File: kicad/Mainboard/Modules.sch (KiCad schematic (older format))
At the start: 14 parts, among them U12 GD25Q16CSIGTR, U14 ESP8266EX, Y1 24MHz

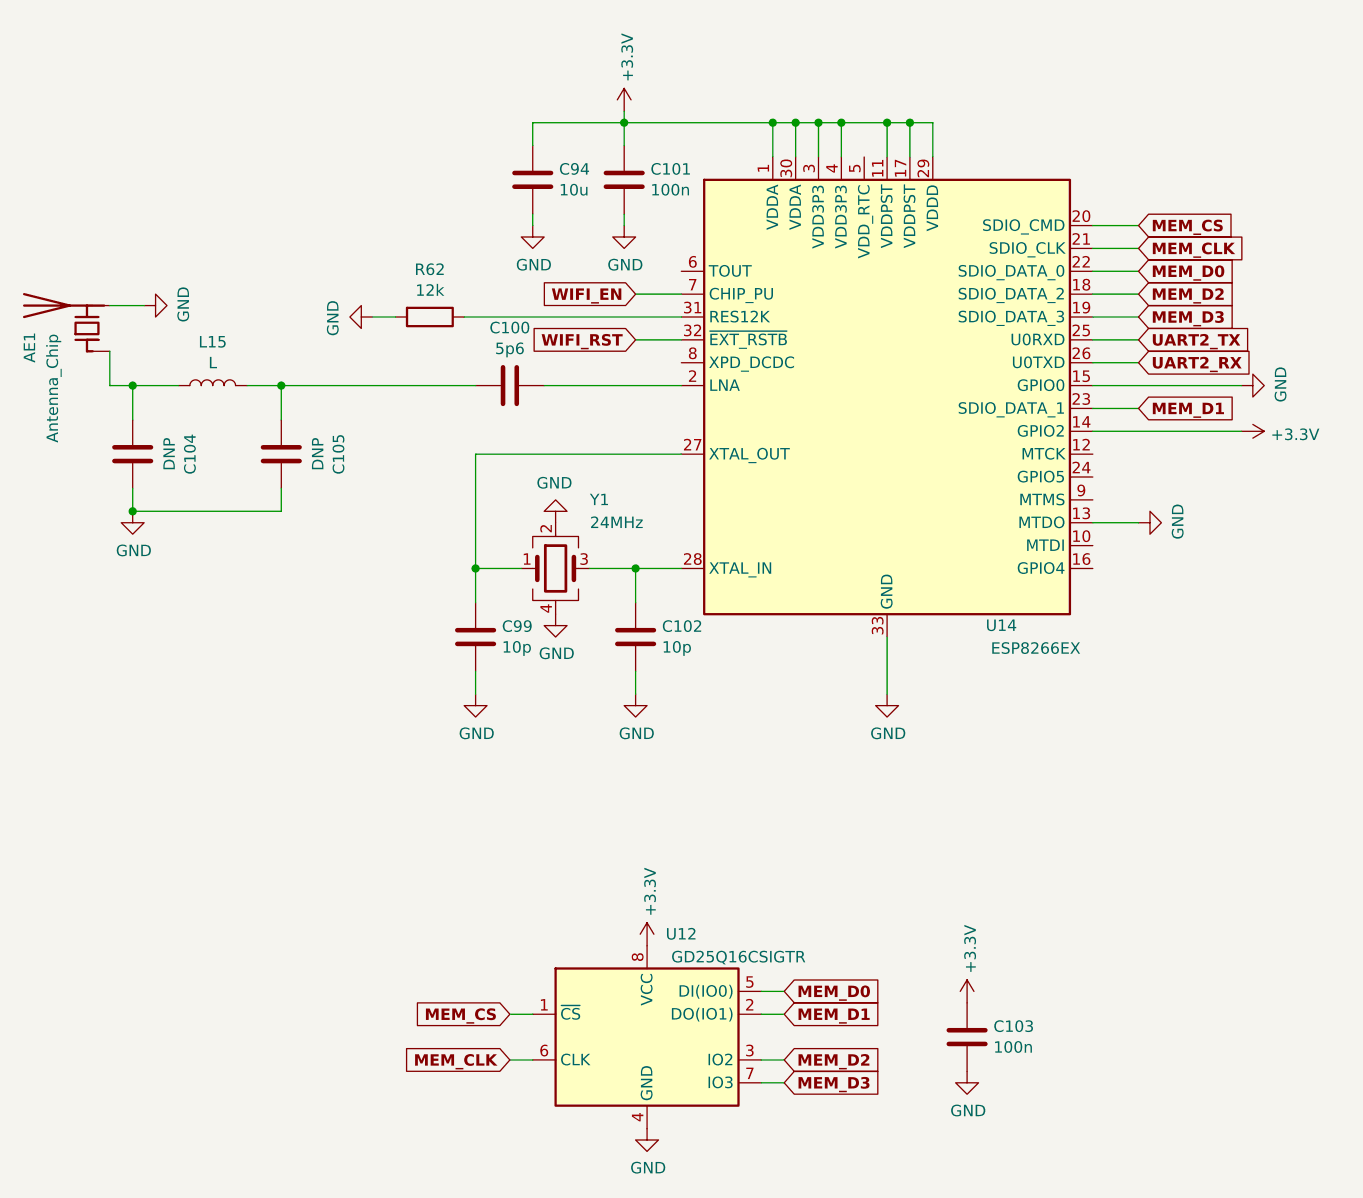
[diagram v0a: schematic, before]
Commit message: removed ESP8266 and it's circuitry; instead added a Pin Headers 2x4 for soldering in ESP8266 SoM; changed vias to manufacturable by JlcPcb; plotted PDF
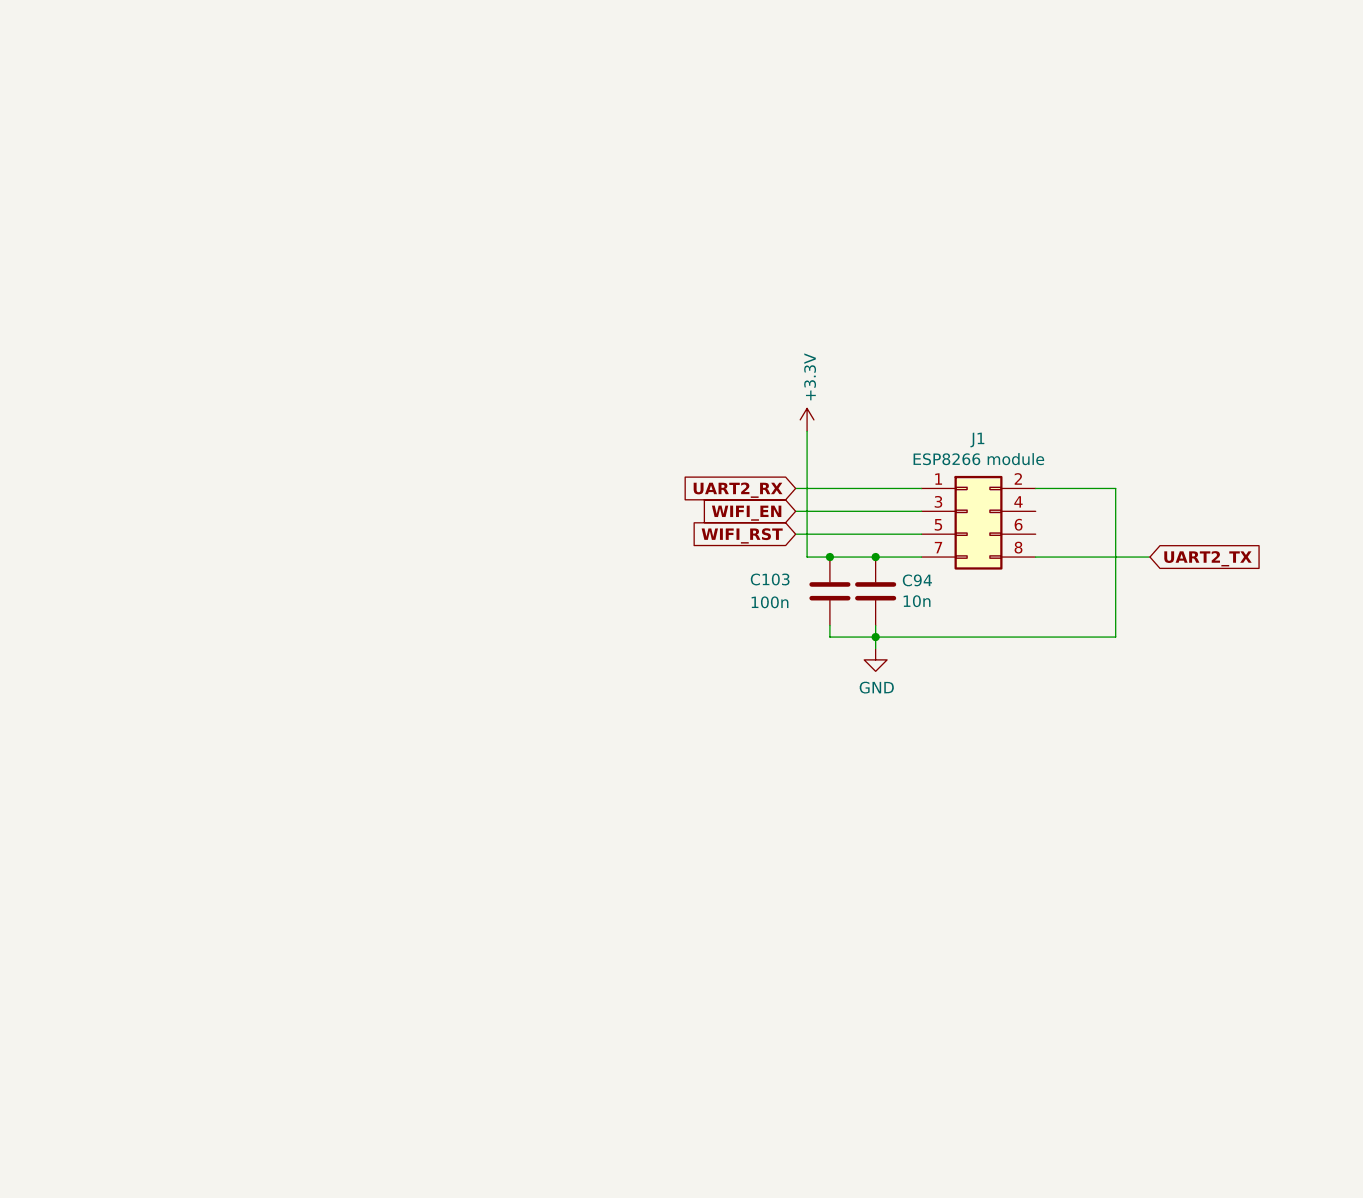
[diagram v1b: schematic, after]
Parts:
- removed AE1: Antenna_Chip, TR-9:RFECA3216060A1T_shifted, symbol Device:Antenna_Chip
- removed C100: 5p6, Inductor_SMD:L_0402_1005Metric, symbol Device:C
- removed C101: 100n, Capacitor_SMD:C_0603_1608Metric, symbol Device:C
- removed C102, C99: 10p, Capacitor_SMD:C_0603_1608Metric, symbol Device:C
- removed C104, C105: DNP, Inductor_SMD:L_0402_1005Metric, symbol Device:C
- removed C94: 10u, Capacitor_SMD:C_0603_1608Metric, symbol Mainboard-rescue:C-Device
- removed L15: L, Inductor_SMD:L_0402_1005Metric, symbol Device:L
- removed R62: 12k, Resistor_SMD:R_0603_1608Metric, symbol Device:R
- removed U12: GD25Q16CSIGTR, Package_SO:SOIC-8_3.9x4.9mm_P1.27mm, symbol Memory_Flash:W25Q32JVSS
- removed U14: ESP8266EX, Package_DFN_QFN:QFN-32-1EP_5x5mm_P0.5mm_EP3.45x3.45mm, symbol MCU_Espressif:ESP8266EX
- removed Y1: 24MHz, Crystal:Crystal_SMD_Abracon_ABM10-4Pin_2.5x2.0mm, symbol Device:Crystal_GND24
- added C94: 10n, Capacitor_SMD:C_0603_1608Metric, symbol Device:C
- added J1: ESP8266 module, Connector_PinHeader_2.54mm:PinHeader_2x04_P2.54mm_Vertical, symbol Connector_Generic:Conn_02x04_Odd_Even
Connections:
- net +3V3: now also C94.1, J1.7 (Pin_7)
- net GND: now also C94.2, J1.2 (Pin_2)
- net UART2_RX: now also J1.1 (Pin_1)
- net UART2_TX: now also J1.8 (Pin_8)
- net WIFI_EN: now also J1.3 (Pin_3)
- net WIFI_RST: now also J1.5 (Pin_5)
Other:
- moved on the sheet: C103

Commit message: some small changes
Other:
- note added: "This is a place for ESP8266 module"
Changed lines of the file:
@@
 Wire Wire Line
 	5800 4800 6000 4800
+Text Notes 5550 5250 0    50   ~ 0
+This is a place for ESP8266 module
+Wire Notes Line
+	5400 5100 5400 5350
+Wire Notes Line
+	7100 5100 7100 5350
+Wire Notes Line
+	7100 5100 5400 5100
+Wire Notes Line
+	5400 5350 7100 5350
 $EndSCHEMATC

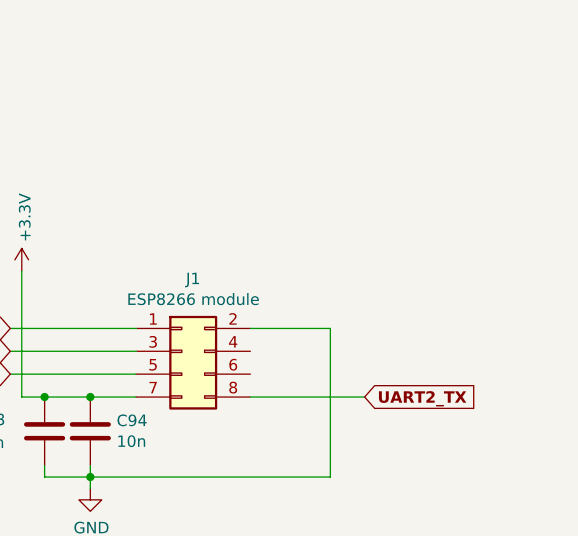
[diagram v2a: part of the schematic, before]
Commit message: added jumpers on GPIO0 and GPIO2 for ESP8266 module; described pin headers on PCB; connected pin 16 of STM32 to Power Down pin in OS1; plotted schematic in PDF
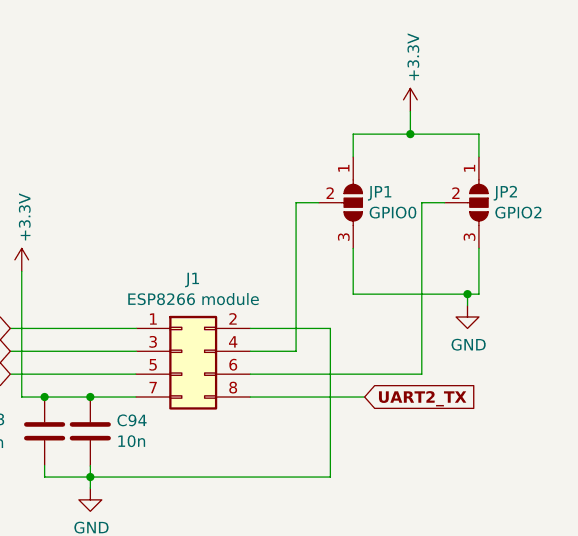
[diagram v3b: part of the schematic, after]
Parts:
- added JP1: GPIO0, Jumper:SolderJumper-3_P1.3mm_Open_RoundedPad1.0x1.5mm, symbol Jumper:SolderJumper_3_Open
- added JP2: GPIO2, Jumper:SolderJumper-3_P1.3mm_Open_RoundedPad1.0x1.5mm, symbol Jumper:SolderJumper_3_Open
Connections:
- net +3V3: now also JP1.1 (A), JP2.1 (A)
- net GND: now also JP1.3 (B), JP2.3 (B)
- net at J1.4 (Pin_4): now also JP1.2 (C)
- net at J1.6 (Pin_6): now also JP2.2 (C)
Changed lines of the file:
@@
 Wire Notes Line
 	5400 5350 7100 5350
+$Comp
+L Jumper:SolderJumper_3_Open JP2
+U 1 1 5F117DC1
+P 7700 3600
+F 0 "JP2" V 7654 3668 50  0000 L CNN
+F 1 "GPIO2" V 7745 3668 50  0000 L CNN
+F 2 "Jumper:SolderJumper-3_P1.3mm_Open_RoundedPad1.0x1.5mm" H 7700 3600 50  0001 C CNN
+F 3 "~" H 7700 3600 50  0001 C CNN
+	1    7700 3600
+	0    1    1    0
+$EndComp
+$Comp
+L Jumper:SolderJumper_3_Open JP1
+U 1 1 5F119F3E
+P 7150 3600
+F 0 "JP1" V 7104 3668 50  0000 L CNN
+F 1 "GPIO0" V 7195 3668 50  0000 L CNN
+F 2 "Jumper:SolderJumper-3_P1.3mm_Open_RoundedPad1.0x1.5mm" H 7150 3600 50  0001 C CNN
+F 3 "~" H 7150 3600 50  0001 C CNN
+	1    7150 3600
+	0    1    1    0
+$EndComp
+Wire Wire Line
+	7000 3600 6900 3600
+Wire Wire Line
+	6900 3600 6900 4250
+Wire Wire Line
+	6900 4250 6700 4250
+Wire Wire Line
+	7550 3600 7450 3600
+Wire Wire Line
+	7450 3600 7450 4350
+Wire Wire Line
+	7450 4350 6700 4350
+Wire Wire Line
+	7700 3800 7700 4000
+Wire Wire Line
+	7700 4000 7650 4000
+Wire Wire Line
+	7150 4000 7150 3800
+Wire Wire Line
+	7700 3400 7700 3300
+Wire Wire Line
+	7700 3300 7400 3300
+Wire Wire Line
+	7150 3300 7150 3400
+$Comp
+L power:+3.3V #PWR0171
+U 1 1 5F11BC56
+P 7400 3200
+F 0 "#PWR0171" H 7400 3050 50  0001 C CNN
+F 1 "+3.3V" V 7415 3328 50  0000 L CNN
+F 2 "" H 7400 3200 50  0001 C CNN
+F 3 "" H 7400 3200 50  0001 C CNN
+	1    7400 3200
+	1    0    0    -1
+$EndComp
+Wire Wire Line
+	7400 3200 7400 3300
+Connection ~ 7400 3300
+Wire Wire Line
+	7400 3300 7150 3300
+$Comp
+L power:GND #PWR0172
+U 1 1 5F11C453
+P 7650 4050
+F 0 "#PWR0172" H 7650 3800 50  0001 C CNN
+F 1 "GND" H 7655 3877 50  0000 C CNN
+F 2 "" H 7650 4050 50  0001 C CNN
+F 3 "" H 7650 4050 50  0001 C CNN
+	1    7650 4050
+	1    0    0    -1
+$EndComp
+Wire Wire Line
+	7650 4050 7650 4000
+Connection ~ 7650 4000
+Wire Wire Line
+	7650 4000 7150 4000
 $EndSCHEMATC
